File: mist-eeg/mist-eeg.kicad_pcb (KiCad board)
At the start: 4 copper layers, 100 x 100 mm, 231 parts, among them J1 Power_5V-14V, J3 Micro_SD_Card_Det, J6 Audio, J7 Electrodes, Q1 20V @ 3A PMOS, SW1 SD_RST, SW3 SW_DIP_x08, SW4 START, SW5 RESET, U1 LTC2947, U12 LT3042xMSE, U13 LT3042xMSE, U14 TPS84A20, U2 LTC4412HV, U22 ADAU1372, U24 ADS1299, U3 SST25VF010A, U4 TPS65987DDJ, U9 TPS63070, Y1 12.288 MHz @ max 20 pF

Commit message: Hooked-up the SoM
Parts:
- removed H3, H4: MountingHole, MountingHole:MountingHole_2.7mm_M2.5_Pad
- removed R150, R151, R152, R153, R154, R155, R156, R157: 10k, Resistor_SMD:R_0603_1608Metric
- removed SW3: SW_DIP_x08, Button_Switch_THT:SW_DIP_SPSTx08_Piano_10.8x21.88mm_W7.62mm_P2.54mm
- added R2: 4k7, Resistor_SMD:R_0201_0603Metric, F.Cu at (20.1, 61.3)
- added SW2: USER, Connector_PinHeader_1.27mm:PinHeader_1x02_P1.27mm_Vertical, F.Cu at (16.8, 62.1)

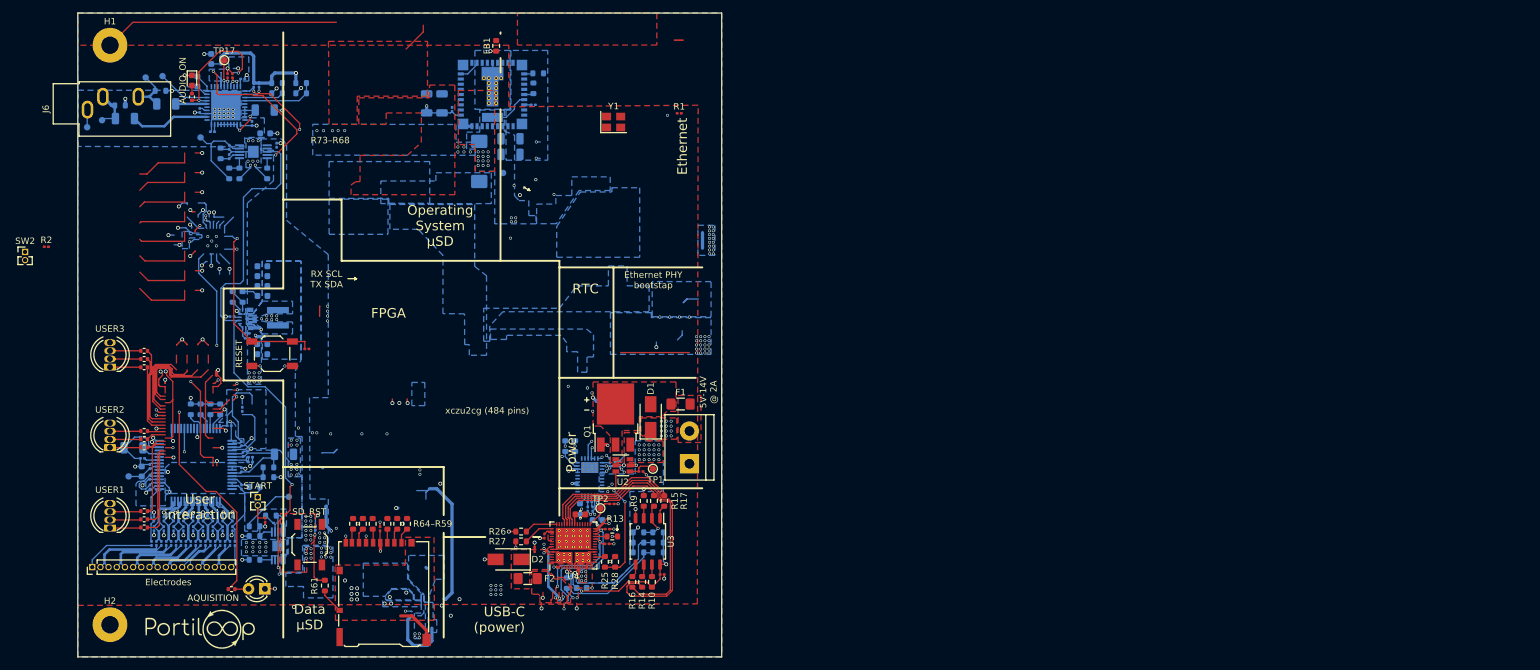
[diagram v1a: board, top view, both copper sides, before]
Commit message: Finish schematic and create interface specifications
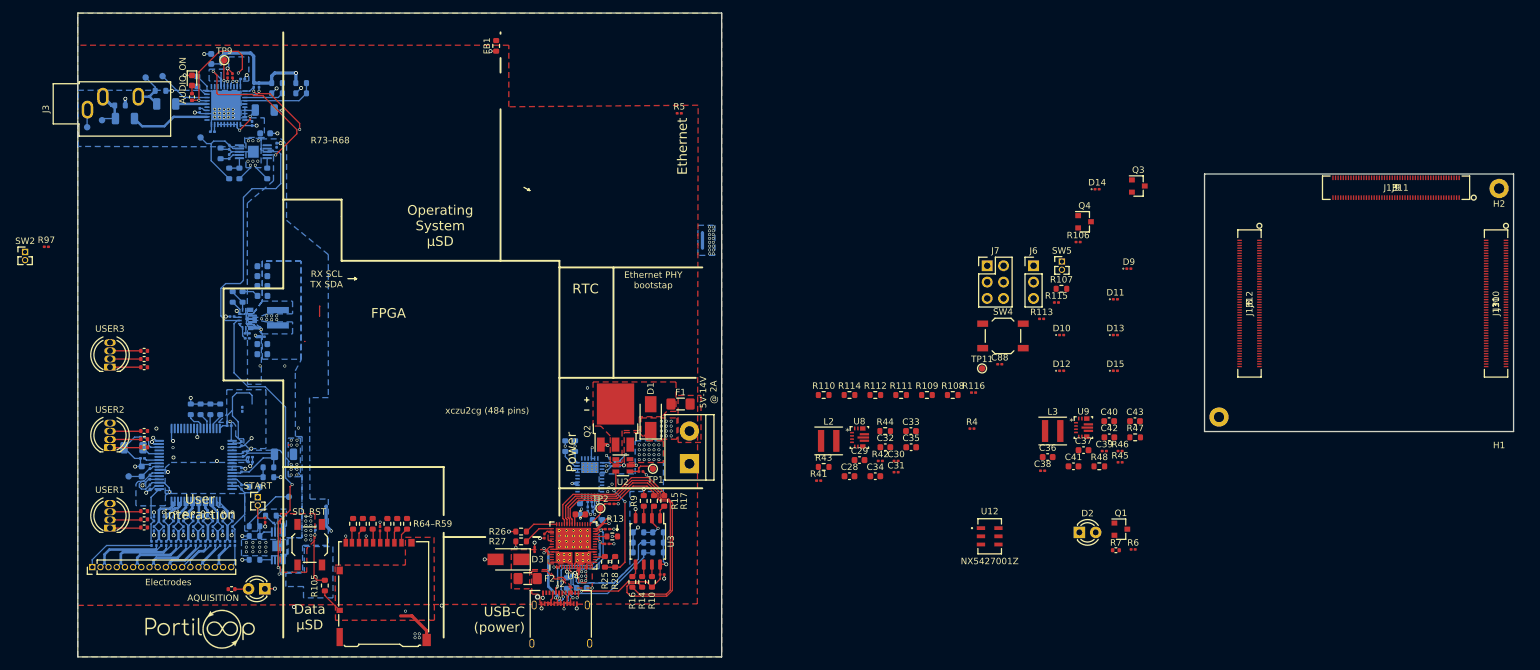
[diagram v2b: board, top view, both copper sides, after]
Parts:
- removed the C68 at (79.2, 39.0)
- removed the C69 at (81.6, 39.0)
- removed the C70 at (83.1, 40.0)
- removed the C71 at (92.2, 44.5)
- removed the C72 at (92.2, 47.0)
- removed the C73 at (87.4, 48.0)
- removed the C74 at (95.7, 39.3)
- removed R162: 4k7, Resistor_SMD:R_0201_0603Metric
- removed the R50 at (95.8, 36.7)
- removed the R51 at (96.5, 34.4)
- removed the TP10 at (91.1, 49.8)
- removed U14: TPS84A20, mist-eeg:TPS84A20
- removed Y1: 12.288 MHz @ max 20 pF, Crystal:Crystal_SMD_Abracon_ABM8G-4Pin_3.2x2.5mm
- added C28: 10uF, Capacitor_SMD:C_0603_1608Metric, F.Cu at (144.9, 96.9)
- added C29: 10uF, Capacitor_SMD:C_0603_1608Metric, F.Cu at (146.4, 94.4)
- added C30: 1uF, Capacitor_SMD:C_0201_0603Metric, F.Cu at (152.1, 94.6)
- added C31: 0u1F, Capacitor_SMD:C_0201_0603Metric, F.Cu at (152.1, 96.3)
- added C32: 10uF, Capacitor_SMD:C_0603_1608Metric, F.Cu at (150.4, 92.4)
- added C33: 22uF, Capacitor_SMD:C_0603_1608Metric, F.Cu at (154.4, 89.9)
- added C34: 22uF, Capacitor_SMD:C_0603_1608Metric, F.Cu at (148.9, 96.9)
- added C35: 22uF, Capacitor_SMD:C_0603_1608Metric, F.Cu at (154.4, 92.4)
- added C36: 10uF, Capacitor_SMD:C_0603_1608Metric, F.Cu at (175.6, 94.0)
- added C37: 10uF, Capacitor_SMD:C_0603_1608Metric, F.Cu at (181.2, 92.9)
- added C38: 1uF, Capacitor_SMD:C_0201_0603Metric, F.Cu at (174.9, 96.1)
- added C39: 0u1F, Capacitor_SMD:C_0201_0603Metric, F.Cu at (184.4, 93.0)
- added C40: 10uF, Capacitor_SMD:C_0603_1608Metric, F.Cu at (185.2, 88.4)
- added C41: 22uF, Capacitor_SMD:C_0603_1608Metric, F.Cu at (179.6, 95.4)
- added C42: 22uF, Capacitor_SMD:C_0603_1608Metric, F.Cu at (185.2, 90.9)
- added C43: 22uF, Capacitor_SMD:C_0603_1608Metric, F.Cu at (189.2, 88.4)
- added C88: 0u1F, Capacitor_SMD:C_0201_0603Metric, F.Cu at (168.2, 79.5)
- added D10: TPD1E6B06DPLR, Diode_SMD:D_0201_0603Metric, F.Cu at (177.8, 75.0)
- added D11: TPD1E6B06DPLR, Diode_SMD:D_0201_0603Metric, F.Cu at (186.2, 69.5)
- added D12: TPD1E6B06DPLR, Diode_SMD:D_0201_0603Metric, F.Cu at (177.8, 80.6)
- added D13: TPD1E6B06DPLR, Diode_SMD:D_0201_0603Metric, F.Cu at (186.2, 75.0)
- added D14: TPD1E6B06DPLR, Diode_SMD:D_0201_0603Metric, F.Cu at (183.3, 52.4)
- added D15: TPD1E6B06DPLR, Diode_SMD:D_0201_0603Metric, F.Cu at (186.2, 80.6)
- added D2: ON, LED_THT:LED_D3.0mm, F.Cu at (180.6, 105.7)
- added D9: TPD1E6B06DPLR, Diode_SMD:D_0201_0603Metric, F.Cu at (188.2, 64.7)
- added J10: J1310, mist-eeg:DF40HC3.0-100DS-0.4V58, F.Cu at (245.3, 70.1)
- added J2: USB_C_Receptacle, Connector_USB:USB_C_Receptacle_Amphenol_12401610E4-2A, F.Cu at (100.0, 120.1)
- added J6: Extra GPIOs, Connector_PinHeader_2.54mm:PinHeader_1x03_P2.54mm_Vertical, F.Cu at (173.4, 64.2)
- added J7: Digital buses, Connector_PinHeader_2.54mm:PinHeader_2x03_P2.54mm_Vertical, F.Cu at (166.2, 64.2)
- added J8: J1312, mist-eeg:DF40HC3.0-100DS-0.4V58, F.Cu at (207.0, 70.1)
- added J9: J1311, mist-eeg:DF40HC3.0-100DS-0.4V58, F.Cu at (229.8, 52.1)
- added L2: 1u5H, Inductor_SMD:L_Coilcraft_XxL4040, F.Cu at (141.6, 91.5)
- added L3: 1u5H, Inductor_SMD:L_Coilcraft_XxL4040, F.Cu at (176.4, 89.9)
- added Q1: NMOS_DGS (5V), Package_TO_SOT_SMD:SOT-23, F.Cu at (187.0, 105.2)
- added Q3: NMOS_DGS (3.3V), Package_TO_SOT_SMD:SOT-23, F.Cu at (189.7, 51.9)
- added Q4: PMOS_DGS (3.3V @ 1A), Package_TO_SOT_SMD:SOT-23, F.Cu at (181.4, 57.4)
- added R106: 4k7, Resistor_SMD:R_0201_0603Metric, F.Cu at (180.4, 60.6)
- added R107: 0R, Resistor_SMD:R_0603_1608Metric, F.Cu at (177.8, 67.8)
- added R108: DNF, Resistor_SMD:R_0603_1608Metric, F.Cu at (160.9, 84.3)
- added R109: DNF, Resistor_SMD:R_0603_1608Metric, F.Cu at (156.9, 84.3)
- added R110: 0R, Resistor_SMD:R_0603_1608Metric, F.Cu at (140.8, 84.3)
- added R111: DNF, Resistor_SMD:R_0603_1608Metric, F.Cu at (152.9, 84.3)
- added R112: DNF, Resistor_SMD:R_0603_1608Metric, F.Cu at (148.9, 84.3)
- added R113: 4k7, Resistor_SMD:R_0201_0603Metric, F.Cu at (174.7, 72.5)
- added R114: DNF, Resistor_SMD:R_0603_1608Metric, F.Cu at (144.9, 84.3)
- added R115: 4k7, Resistor_SMD:R_0201_0603Metric, F.Cu at (177.0, 70.0)
- added R116: 4k7, Resistor_SMD:R_0201_0603Metric, F.Cu at (164.1, 83.9)
- added R4: 4k7, Resistor_SMD:R_0201_0603Metric, F.Cu at (163.9, 89.5)
- added R41: 4k7, Resistor_SMD:R_0201_0603Metric, F.Cu at (140.1, 97.6)
- added R42: 4k7, Resistor_SMD:R_0201_0603Metric, F.Cu at (149.6, 94.6)
- added R43: 31k3, Resistor_SMD:R_0603_1608Metric, F.Cu at (140.8, 95.5)
- added R44: 10k, Resistor_SMD:R_0603_1608Metric, F.Cu at (150.4, 89.9)
- added R45: 4k7, Resistor_SMD:R_0201_0603Metric, F.Cu at (186.9, 94.8)
- added R46: 4k7, Resistor_SMD:R_0201_0603Metric, F.Cu at (186.9, 93.0)
- added R47: 52k5, Resistor_SMD:R_0603_1608Metric, F.Cu at (189.2, 90.9)
- added R48: 10k, Resistor_SMD:R_0603_1608Metric, F.Cu at (183.7, 95.4)
- added R6: 4k7, Resistor_SMD:R_0201_0603Metric, F.Cu at (188.9, 108.3)
- added R7: 1k, Resistor_SMD:R_0402_1005Metric, F.Cu at (186.2, 108.4)
- added SW4: RESET, Button_Switch_SMD:SW_SPST_TL3342, F.Cu at (168.7, 75.1)
- added TP11: ~POR~, TestPoint:TestPoint_Pad_D1.0mm, F.Cu at (165.4, 80.2)
- added U12: NX5427001Z, mist-eeg:NX5427001Z, F.Cu at (166.6, 106.3)
- added U8: TPS63070, mist-eeg:TPS630702RNMR, F.Cu at (146.4, 90.9)
- added U9: TPS63070, mist-eeg:TPS630702RNMR, F.Cu at (181.2, 89.4)
- H1, H2: footprint MountingHole:MountingHole_2.7mm_M2.5_Pad -> mist-eeg:MountingHole_1.6mm
- SW5: value RESET -> ONOFF; footprint Button_Switch_SMD:SW_SPST_TL3342 -> Connector_PinHeader_1.27mm:PinHeader_1x02_P1.27mm_Vertical
- moved H2 226.1 mm to (245.8, 52.2)
- moved H1 223.9 mm to (245.8, 89.8)
- moved SW5 123.5 mm to (177.8, 63.6)
- renumbered C48 to C14, C49 to C15, C50 to C16, C51 to C17, C52 to C18, C53 to C19, C54 to C20, C55 to C21, C62 to C22, C63 to C23, C64 to C24, C65 to C25, C66 to C26, C67 to C27, C109 to C44, C110 to C45, C111 to C46, C112 to C47, C113 to C48, C114 to C49, C115 to C50, C116 to C51, C117 to C52, C118 to C53, C119 to C54, C121 to C55, C120 to C56, C123 to C57, C122 to C58, C124 to C59, C125 to C60, C126 to C61, C127 to C62, C128 to C63, C129 to C64, C130 to C65, C131 to C66, C132 to C67, C133 to C68, C134 to C69, C135 to C70, C136 to C71, C137 to C72, C138 to C73, C139 to C74, C140 to C75, C141 to C76, C142 to C77, C143 to C78, C144 to C79, C145 to C80, C146 to C81, C147 to C82, C148 to C83, C149 to C84, C150 to C85, C151 to C86, C81 to C87, D2 to D3, D7 to D5, D10 to D6, D11 to D7, D12 to D8, J6 to J3, J7 to J4, J3 to J5, L3 to L1, Q1 to Q2, R3 to R1, R56 to R100, R57 to R101, R58 to R102, R59 to R103, R60 to R104, R61 to R105, R4 to R2, R38 to R29, R5 to R3, R39 to R30, R40 to R31, R41 to R32, R42 to R33, R43 to R34, R44 to R35, R45 to R36, R46 to R37, R47 to R38, R48 to R39, R49 to R40, R100 to R49, R1 to R5, R101 to R50, R102 to R51, R103 to R52, R104 to R53, R105 to R54, R106 to R55, R107 to R56, R108 to R57, R109 to R58, R110 to R59, R114 to R60, R115 to R61, R116 to R62, R117 to R63, R113 to R64, R118 to R65, R119 to R66, R120 to R67, R121 to R68, R122 to R69, R123 to R70, R124 to R71, R125 to R72, R126 to R73, R127 to R74, R128 to R75, R129 to R76, R130 to R77, R131 to R78, R132 to R79, R6 to R8, R133 to R80, R134 to R81, R135 to R82, R136 to R83, R137 to R84, R138 to R85, R141 to R86, R144 to R87, R145 to R88, R146 to R89, R147 to R90, R148 to R91, R149 to R92, R158 to R93, R159 to R94, R160 to R95, R161 to R96, R2 to R97, R54 to R98, R55 to R99, SW4 to SW1, SW1 to SW3, TP18 to TP10, TP8 to TP3, TP9 to TP4, TP13 to TP5, TP14 to TP6, TP15 to TP7, TP16 to TP8, TP17 to TP9, U22 to U10, U24 to U11, U9 to U5, U12 to U6, U13 to U7
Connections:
- net /SD_DATA_CONNECTED renamed /~SD_CONNECTED~
- net /power/5V25/ENA renamed Net-(R30-Pad2)
- C87 pad 1: +3V3 -> /SD_DATA/+PWR
- J5 pad 4: +3V3 -> /SD_DATA/+PWR
- R100 pad 2: (no net) -> /SD_DAT1
- R101 pad 2: (no net) -> /SD_DAT2
- R102 pad 2: (no net) -> /SD_DAT3
- R103 pad 2: (no net) -> /SD_CMD
- R104 pad 2: (no net) -> /SD_CLK
- R5 pad 2: /power/STAGE_2 -> /AUDIO_PWR_OK
- R86 pad 2: (no net) -> /AQUISITION
- R87 pad 2: (no net) -> /USER1_R
- R88 pad 2: (no net) -> /USER1_G
- R89 pad 2: (no net) -> /USER1_B
- R90 pad 2: (no net) -> /USER3_R
- R91 pad 2: (no net) -> /USER3_G
- R92 pad 2: (no net) -> /USER3_B
- R93 pad 2: (no net) -> /USER2_R
- R94 pad 2: (no net) -> /USER2_G
- R95 pad 2: (no net) -> /USER2_B
- R99 pad 2: (no net) -> /SD_DAT0
- SW3 pad 2: +3V3 -> Net-(Q4-Pad3)
- SW5 pad 1: /~RESET~ -> GND
- SW5 pad 2: GND -> /SoM/ONOFF
- U10 pad 31: (no net) -> /AUDIO_LRCLK
- U10 pad 32: (no net) -> /AUDIO_BCLK
- U10 pad 33: (no net) -> /AUDIO_SDATA
- U10 pad 34: (no net) -> /AUDIO_PWR_OK
- U10 pad 38: /audio/XO -> (no net)
- U10 pad 39: /audio/XI -> /AUDIO_MCLK
- U11 pad 34: (no net) -> /EEG_MOSI
- U11 pad 35: (no net) -> /~EEG_PWDN~
- U11 pad 36: (no net) -> /~EEG_RESET~
- U11 pad 38: (no net) -> /EEG_START
- U11 pad 39: (no net) -> /~EEG_CS~
- U11 pad 40: (no net) -> /EEG_SCK
- U11 pad 43: (no net) -> /EEG_MISO
- U11 pad 47: (no net) -> /~EEG_DRDY~
- U4 pad 50: (no net) -> /power/USB/DP
- U4 pad 53: (no net) -> /power/USB/DN
- U6 pad 4: /power/STAGE_2 -> /AUDIO_PWR_OK
- U7 pad 4: /power/STAGE_2 -> /AUDIO_PWR_OK
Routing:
- net (no net): track 182.1 -> 0.00 mm, vias 8 -> 0
- net GND: track 233.4 -> 171.1 mm, vias 269 -> 184
- net SHIELD: track 49.2 -> 6.43 mm
- net /audio/XI: track 30.4 -> 0.00 mm, vias 2 -> 0
- net /~RESET~: track 29.7 -> 0.01 mm, vias 1 -> 0
- net +3V3: track 79.2 -> 52.5 mm, vias 37 -> 16
- net +PL_HD: track 24.4 -> 0.00 mm, vias 12 -> 0
- net +DDR_VDD2: track 23.9 -> 0.00 mm
- net Net-(U14-Pad10): track 17.7 -> 0.00 mm
- net /user-interaction/~ENA~: track 16.4 -> 0.00 mm, vias 2 -> 0
- net /user-interaction/PS_STATUS_O: track 14.7 -> 0.00 mm
- net /user-interaction/PS_ERR_O: track 13.9 -> 0.00 mm
- net /user-interaction/PS_INIT_O: track 13.7 -> 0.00 mm
- net /power/USB/DN: track 0.00 -> 13.6 mm, vias 0 -> 3
- net /power/USB/DP: track 0.00 -> 12.2 mm, vias 0 -> 2
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- added copper zone on B.Cu, net Net-(L3-Pad1)
- added copper zone on B.Cu, net Net-(L3-Pad2)
- removed copper zone on B.Cu, net +0V85
- removed copper zone on B.Cu, net +1V0
- removed copper zone on B.Cu, net +1V2
- removed copper zone on B.Cu, net +2V5
- removed copper zone on B.Cu, net +MIO
- removed copper zone on In2.Cu, net +MIO
- removed copper zone on B.Cu, net +VCCINT
- removed copper zone on B.Cu, net /FPGA/FPGA_power/PSDDR_PLL
- removed copper zone on F.Cu, net /SD_OS/+PWR
- removed copper zone on B.Cu, net /power/DDR-power/SW
- removed copper zone on F.Cu, net Net-(FB2-Pad1)
- removed copper zone on B.Cu, net Net-(L1-Pad1)
- removed copper zone on B.Cu, net Net-(L1-Pad2)
- removed copper zone on B.Cu, net Net-(L2-Pad1)
- removed copper zone on B.Cu, net Net-(R229-Pad2)
- removed copper zone on B.Cu, net Net-(U14-Pad10)
- removed copper zone on B.Cu, net Net-(U6-Pad10)
- removed copper zone on B.Cu, net Net-(U7-Pad10)
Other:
- board size 100 x 100 mm -> 223 x 100 mm

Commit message: Place components
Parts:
- removed C43: 22uF, Capacitor_SMD:C_0603_1608Metric
- C22, C23, C24, C25, C26, C27, C44, C45, C46, C47, C48, C49, C50, C51, C52, C53, R33, R34, R35, R36, R37, R38, R39, R40, R49, R50, R51, R52, R53, R54, R58, R59, R98, TP4, TP8, U10, U6, U7: moved to F.Cu
- D1, D10, D11, D12, D13, D14, D15, D4, D9, F1, J3, J4, Q2, R57, SW4, SW5, TP9: moved to B.Cu
- moved J4 226.2 mm to (246.8, 56.5)
- moved TP10 209.9 mm to (241.1, 70.6), turned to 90 degrees
- moved C65 207.4 mm to (240.3, 75.1), turned to 180 degrees
- moved R65 206.6 mm to (237.6, 60.2), turned to 90 degrees
- moved C86 205.7 mm to (239.1, 71.4), turned to 270 degrees
- moved R67 205.1 mm to (236.8, 60.2), turned to 90 degrees
- moved C59 205.0 mm to (239.0, 73.4), turned to 180 degrees
- moved C68 204.8 mm to (237.2, 62.5), turned to 90 degrees
- moved C64 204.4 mm to (239.0, 76.7), turned to 180 degrees
- moved C66 204.2 mm to (237.2, 64.0), turned to 270 degrees
- moved C55 203.8 mm to (237.8, 69.0), turned to 90 degrees
- moved R68 203.6 mm to (236.0, 60.2), turned to 90 degrees
- moved C57 203.4 mm to (237.8, 70.5), turned to 90 degrees
- moved C85 203.0 mm to (237.8, 72.1), turned to 270 degrees
- moved R69 202.1 mm to (235.3, 60.2), turned to 90 degrees
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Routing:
- net /power/STAGE_1: track 107.0 -> 20.3 mm, vias 3 -> 0
- net /SD_CMD: track 0.00 -> 53.1 mm, vias 0 -> 1
- net /SD_CLK: track 0.00 -> 48.2 mm, vias 0 -> 1
- net /SD_DAT3: track 0.00 -> 47.2 mm, vias 0 -> 1
- net /SD_DAT1: track 0.00 -> 46.4 mm, vias 0 -> 1
- net /SD_DAT2: track 0.41 -> 45.8 mm, vias 0 -> 1
- net /SD_DAT0: track 0.00 -> 44.1 mm, vias 0 -> 3
- net /AUDIO_PWR_OK: track 30.1 -> 1.33 mm, vias 2 -> 1
- net +3V3: track 52.5 -> 24.2 mm, vias 16 -> 0
- net GND: track 171.1 -> 152.1 mm, vias 184 -> 97
- net /~AUDIO_PWDN~: track 18.2 -> 2.37 mm, vias 2 -> 1
- net /power/+EXT_IN: track 0.00 -> 15.6 mm, vias 0 -> 1
- net /AUDIO_SDA: track 12.4 -> 1.63 mm, vias 2 -> 0
- net /CTRL_SCL: track 10.6 -> 2.74 mm, vias 2 -> 1
- net /SoM/CLK+: track 0.00 -> 7.25 mm, vias 0 -> 2
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- added copper zone on F.Cu, net /+1V8_ANA
- added copper zone on F.Cu, net /+5V_SOM
- added copper zone on B.Cu, net /power/+EXT_IN
- added copper zone on In2.Cu, net GND
- added copper zone on F.Cu, net Net-(L2-Pad1)
- added copper zone on F.Cu, net Net-(L2-Pad2)
- removed copper zone on In2.Cu, net +3V3
- removed copper zone on B.Cu, net +DDR_VDD1
- removed copper zone on B.Cu, net +PL_HD
- removed copper zone on B.Cu, net /+1V8_ANA
- removed copper zone on B.Cu, net /power/+5V25
- removed copper zone on F.Cu, net /power/+EXT_IN
- removed copper zone on F.Cu, net Net-(F1-Pad2)
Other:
- board size 223 x 100 mm -> 50 x 75 mm

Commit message: Advance routing
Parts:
- removed C10: 1uF, Capacitor_SMD:C_0201_0603Metric
- removed C11, C7: 220pF, Capacitor_SMD:C_0201_0603Metric
- removed C12: 0u1F, Capacitor_SMD:C_0201_0603Metric
- removed C13, C8, C9: 10uF, Capacitor_SMD:C_0603_1608Metric
- removed D3: D_Zener_Small, Diode_SMD:D_SMA
- removed F2: 5V @ 3A, Fuse:Fuse_1206_3216Metric_Pad1.42x1.75mm_HandSolder
- removed J2: USB_C_Receptacle, Connector_USB:USB_C_Receptacle_Amphenol_12401610E4-2A
- removed Q2: 20V @ 3A PMOS, Package_TO_SOT_SMD:TO-252-3_TabPin2
- removed R10, R13, R14, R15, R16, R17, R18, R19, R22, R25, R9: 0R, Resistor_SMD:R_0603_1608Metric
- removed R11, R12, R46: 4k7, Resistor_SMD:R_0201_0603Metric
- removed R20, R23, R28: 10k, Resistor_SMD:R_0603_1608Metric
- removed R21, R24, R26, R27: DNF, Resistor_SMD:R_0603_1608Metric
- removed TP1: EXT_IN, TestPoint:TestPoint_Pad_D1.0mm
- removed TP2: USB_RST, TestPoint:TestPoint_Pad_D1.0mm
- removed U2: LTC4412HV, Package_TO_SOT_SMD:SOT-23-6
- removed U3: SST25VF010A, Package_SO:SOIC-8_5.275x5.275mm_P1.27mm
- removed U4: TPS65987DDJ, mist-eeg:TPS65987DDJ
- C44, C45, R110, R111, R112, R113, R114, R115, R51, R52, TP11: moved to B.Cu
- J3, SW5, TP3, TP5, TP6, TP7: moved to F.Cu
- R8: value 4k7 -> DNF; footprint Resistor_SMD:R_0201_0603Metric -> Resistor_SMD:R_1206_3216Metric; moved to B.Cu
- moved G*** 174.4 mm to (218.2, 113.7)
- moved G*** 130.0 mm to (211.0, 118.0)
- moved REF** 120.3 mm to (230.7, 119.6)
- moved R110 96.3 mm to (237.2, 82.9)
- moved D7 89.7 mm to (243.1, 38.1), turned to 0 degrees
- moved D8 84.7 mm to (235.6, 38.1), turned to 0 degrees
- moved R108 84.5 mm to (245.4, 83.2), turned to 270 degrees
- moved R111 84.3 mm to (237.2, 84.5)
- moved R92 84.3 mm to (245.6, 42.4), turned to 270 degrees
- moved R91 83.1 mm to (244.3, 42.4), turned to 270 degrees
- moved D6 82.1 mm to (228.1, 38.1), turned to 0 degrees
- moved D5 82.1 mm to (222.1, 38.1), turned to 0 degrees
- moved R90 81.9 mm to (243.1, 42.4), turned to 270 degrees
- moved TP11 79.9 mm to (245.2, 76.8)
- moved R95 78.0 mm to (238.1, 42.4), turned to 270 degrees
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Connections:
- C32 pad 1: +3V3 -> /+3V3_SD
- C33 pad 1: +3V3 -> /+3V3_SD
- C34 pad 1: +3V3 -> /+3V3_SD
- C35 pad 1: +3V3 -> /+3V3_SD
- D1 pad 2: /power/+EXT_IN -> /power/+PWR_IN
- F1 pad 1: /power/+EXT_IN -> /power/+PWR_IN
- FB1 pad 2: SHIELD -> Net-(FB1-Pad2)
- H1 pad 1: SHIELD -> (no net)
- H2 pad 1: SHIELD -> (no net)
- J10 pad 10: /USER3_R -> /USER3_B
- J10 pad 16: /USER3_B -> /USER3_R
- J5 pad 11: SHIELD -> Net-(FB1-Pad2)
- J7 pad 1: /CTRL_SDA -> /SoM/TXD
- J7 pad 2: /CTRL_SCL -> /SoM/RXD
- J7 pad 4: /SoM/TXD -> GND
- J7 pad 5: /SoM/RXD -> /CTRL_SDA
- J7 pad 6: GND -> /CTRL_SCL
- Q1 pad 1: /+5V_SOM -> +3V3
- R106 pad 1: +3V3 -> /+3V3_SD
- R109 pad 1: +3V3 -> /+3V3_SD
- R112 pad 2: /SoM/VDD_3V3 -> +3V3
- R114 pad 2: /SoM/VDD_3V3 -> +3V3
- R43 pad 1: +3V3 -> /+3V3_SD
- R6 pad 2: /+5V_SOM -> +3V3
- R8 pad 1: +3V3 -> /power/+PWR
- R8 pad 2: Net-(R8-Pad2) -> /power/+PWR_IN
- SW3 pad 1: +3V3 -> /+3V3_SD
- U8 pad 7: +3V3 -> /+3V3_SD
- U8 pad 8: +3V3 -> /+3V3_SD
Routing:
- net GND: track 152.1 -> 290.0 mm, vias 97 -> 196
- net /CTRL_SCL: track 2.74 -> 81.4 mm, vias 1 -> 4
- net /CTRL_SDA: track 5.50 -> 80.0 mm, vias 2 -> 4
- net /power/+5V25: track 7.75 -> 66.8 mm, vias 2 -> 1
- net /USER3_B: track 0.00 -> 54.7 mm
- net /USER3_R: track 0.00 -> 54.4 mm
- net /USER3_G: track 0.00 -> 54.2 mm
- net /AUDIO_PWR_OK: track 1.33 -> 54.9 mm, vias 1 -> 4
- net /SoM/~PWR_ON~: track 0.00 -> 53.5 mm, vias 0 -> 1
- net /START: track 0.00 -> 52.8 mm
- net /~SD_RST~: track 0.00 -> 50.8 mm, vias 0 -> 2
- net Net-(R14-Pad1): track 48.1 -> 0.00 mm
- net /SoM/~RESET~: track 0.00 -> 42.6 mm, vias 0 -> 3
- net Net-(R16-Pad1): track 42.2 -> 0.00 mm
- net /EEG_MOSI: track 0.00 -> 39.3 mm, vias 0 -> 3
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- added copper zone on F.Cu, net /+3V3_SD
- added copper zone on F.Cu, net /+5V0_ANA
- added copper zone on F.Cu, net /SD_DATA/+PWR
- added copper zone on B.Cu, net /power/+5V25
- added copper zone on F.Cu, net /power/+PWR
- added copper zone on B.Cu, net Net-(F1-Pad2)
- added copper zone on F.Cu, net Net-(FB1-Pad2)
- added copper zone on B.Cu, net Net-(L1-Pad1)
- added copper zone on B.Cu, net Net-(L1-Pad2)
- added copper zone on F.Cu, net Net-(L3-Pad1)
- added copper zone on F.Cu, net Net-(L3-Pad2)
- removed copper zone on B.Cu, net /power/+EXT_IN
- removed copper zone on F.Cu, net /power/+PWR_IN
- removed copper zone on F.Cu, net /power/USB/+USB_5V
- removed copper zone on F.Cu, net /power/USB/+VBUS
- removed copper zone on B.Cu, net Net-(L3-Pad1)
- removed copper zone on B.Cu, net Net-(L3-Pad2)
- removed copper zone on F.Cu, net SHIELD
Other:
- board text removed: "0.85V Regulator"
- board text removed: "1.2V Regulator"
- board text removed: "1.8V Regulator"
- board text removed: "3.3V Regulator"
- board text removed: "5.25V Regulator"
- board text removed: "Audio"
- board text removed: "CMOS batt"
- board text removed: "Clocks"
- board text removed: "DDR Regulators"
- board text removed: "Data μSD"
- board text removed: "Decoupling & config"
- board text removed: "EEG frontend"
- board text removed: "Ethernet"
- board text removed: "Ethernet PHY bootstap"
- board text removed: "Ethernet Regulators"
- board text removed: "FPGA"
- board text removed: "Input conditioning"
- board text removed: "Operating System μSD"
- board text removed: "Power"
- board text removed: "Power Input & Measurement"
- board text removed: "R64–R59"
- board text removed: "R73–R68"
- board text removed: "RTC"
- board text removed: "RX SCL TX SDA"
- board text removed: "USB-C (power)"
- board text removed: "User interaction"
- board text removed: "VCCINT Regulator"
- board text removed: "xczu2cg (484 pins)"

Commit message: Finished layout
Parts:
- G***: moved to B.Cu
- moved G*** 73.1 mm to (238.1, 43.4), turned to 180 degrees
- moved G*** 25.3 mm to (225.0, 96.9)
- moved REF** 22.6 mm to (241.7, 99.8)
- moved C22 1.93 mm to (216.2, 64.1), turned to 90 degrees
- moved C53 1.32 mm to (212.5, 67.7)
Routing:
- net /USER1_B: track 0.00 -> 56.6 mm, vias 0 -> 2
- net /USER2_B: track 0.00 -> 55.8 mm, vias 0 -> 2
- net /USER1_G: track 0.00 -> 55.0 mm, vias 0 -> 2
- net /USER2_G: track 0.00 -> 54.0 mm, vias 0 -> 2
- net /USER2_R: track 0.00 -> 53.6 mm, vias 0 -> 2
- net /USER1_R: track 0.00 -> 53.5 mm, vias 0 -> 2
- net /AQUISITION: track 0.00 -> 43.6 mm, vias 0 -> 2
- net /USER: track 1.65 -> 43.8 mm, vias 0 -> 2
- net /SoM/EXTRA_2: track 0.00 -> 40.8 mm
- net /SoM/EXTRA_3: track 0.00 -> 36.4 mm
- net /SoM/EXTRA_1: track 0.00 -> 28.0 mm, vias 0 -> 2
- net /power/STAGE_1: track 38.9 -> 66.1 mm, vias 1 -> 3
- net /power/+5V25: track 66.8 -> 93.6 mm, vias 1 -> 4
- net /AUDIO_PWR_OK: track 54.9 -> 78.0 mm, vias 4 -> 6
- net /AUDIO_MCLK: track 0.00 -> 18.7 mm, vias 0 -> 2
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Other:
- board text added: "1"
- board text added: "Controls RX GND SCL TX 3V3 SDA"
- board text added: "Extra GPIOs"
- board text added: "LEFT"
- board text added: "REF"
- board text added: "RIGHT"
